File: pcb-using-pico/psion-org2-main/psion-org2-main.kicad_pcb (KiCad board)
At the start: 2 copper layers, 70 x 106 mm, 122 parts, among them J1 Conn_01x24_Female, J2 Conn_01x03_Female, J3 Conn_01x27_Female, J4 Conn_01x02_Female, J5 Conn_01x02_Female, J6 Conn_01x11_Female, M1 P-CH-MOSFET, M2 P-CHANNEL-MOSFET, M3 P-CHANNEL-MOSFET, SW1 AC_ON, SW10 n, SW11 t, SW12 del, SW13 up, SW14 c, SW15 i, SW16 o, SW17 u, SW18 y, SW19 down, SW2 A, SW20 d, SW21 j, SW22 p, SW23 v, SW24 z, SW25 left, SW26 e, SW27 k, SW28 q, SW29 w, SW3 g, SW30 spc, SW31 right, SW32 f, SW33 L, SW34 r, SW35 x, SW36 exe, SW4 m, SW5 s, SW6 shft, SW7 mode, SW8 b, SW9 h, U1 Pico, U10 AMS1117-3.3, U2 74HC595, U3 Regulator_Switching_MT3608, U4 74LS165, U5 74HC595, U7 MCP7940N-xSN, Y1 32k768Hz

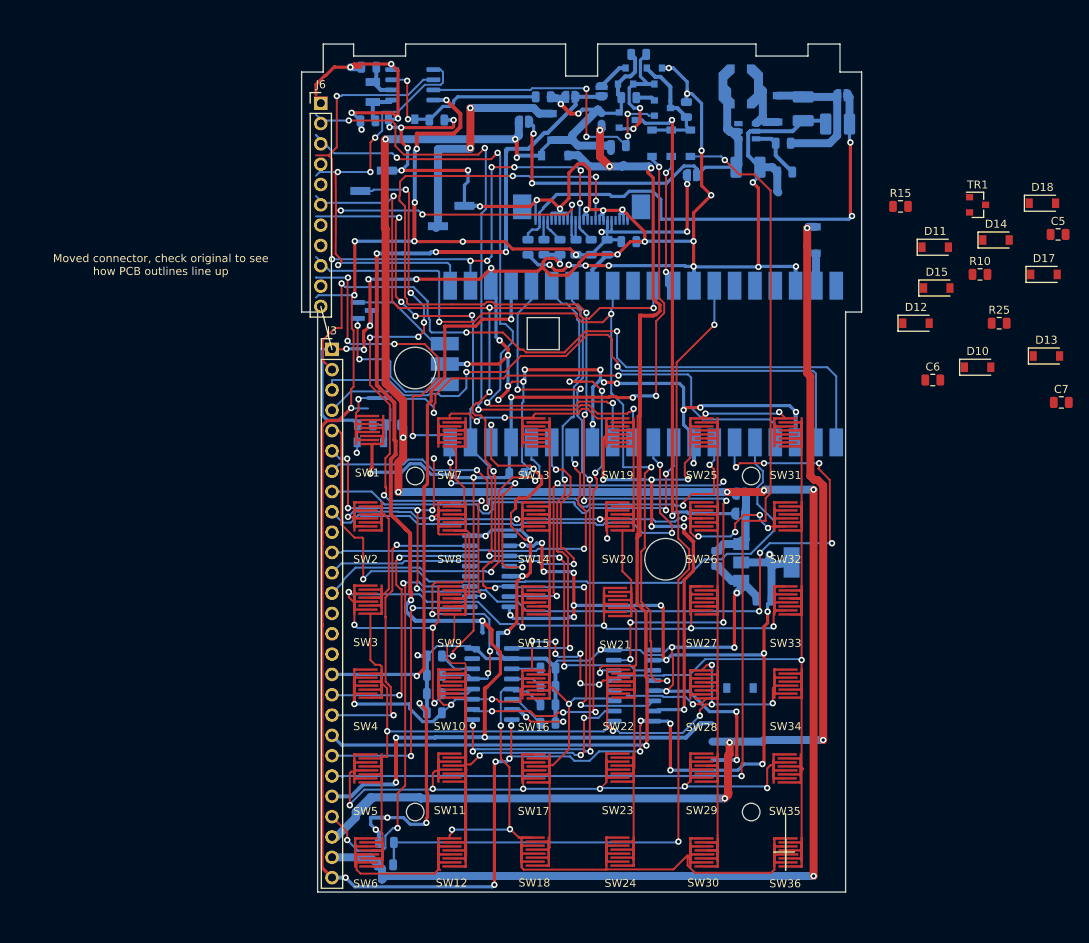
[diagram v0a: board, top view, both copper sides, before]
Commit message: V1.1 PCBs
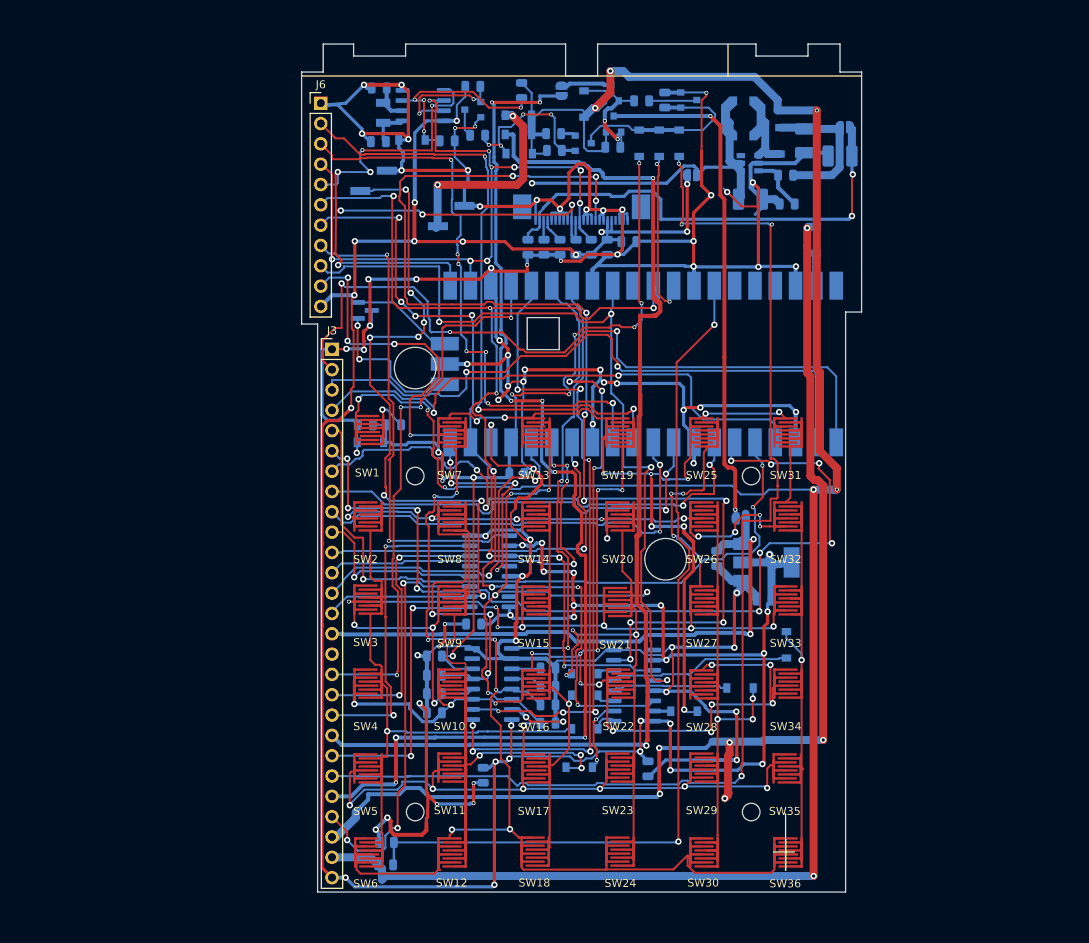
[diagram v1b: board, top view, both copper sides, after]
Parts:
- removed JP3, JP5, JP7: Jumper_NO_Small, Jumper:SolderJumper-2_P1.3mm_Open_RoundedPad1.0x1.5mm
- C5, C6, C7, D10, D11, D12, D13, D14, D15, D17, D18, R10, R15, R25, TR1: moved to B.Cu
- moved C7 86.0 mm to (161.0, 147.1), turned to 270 degrees
- moved C5 84.2 mm to (181.6, 146.3), turned to 270 degrees
- moved D14 84.0 mm to (173.0, 146.1)
- moved D18 82.0 mm to (173.7, 134.4)
- moved D13 74.2 mm to (173.7, 141.3)
- moved R25 72.2 mm to (159.7, 61.0)
- moved D15 67.3 mm to (173.7, 137.1)
- moved R10 65.2 mm to (160.3, 67.1)
- moved C6 65.0 mm to (159.8, 128.2), turned to 180 degrees
- moved TR1 64.2 mm to (159.7, 63.9), turned to 180 degrees
- moved D10 63.2 mm to (165.5, 69.4), turned to 180 degrees
- moved D12 56.5 mm to (186.1, 139.1), turned to 180 degrees
- moved D17 56.4 mm to (198.9, 130.8), turned to 270 degrees
- moved D11 47.4 mm to (173.6, 63.2), turned to 90 degrees
- moved R15 35.0 mm to (180.8, 62.8)
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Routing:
- net P53: track 109.6 -> 192.6 mm, vias 6 -> 12
- net VBAT_SWITCHED1: track 10.4 -> 75.9 mm, vias 0 -> 2
- net QH_O: track 0.00 -> 60.8 mm, vias 0 -> 2
- net P52: track 132.2 -> 186.9 mm, vias 3 -> 7
- net P54: track 121.9 -> 172.5 mm, vias 14 -> 16
- net EXT_PWR_IN: track 207.3 -> 253.9 mm, vias 4 -> 2
- net K6: track 121.3 -> 79.3 mm
- net (no net): track 41.5 -> 0.00 mm, vias 3 -> 0
- net 5V: track 193.7 -> 152.8 mm, vias 4 -> 6
- net VBAT_SWITCHED2: track 174.4 -> 137.5 mm
- net P55: track 146.5 -> 180.0 mm, vias 8 -> 14
- net K4: track 101.3 -> 74.7 mm
- net VBAT: track 285.7 -> 309.4 mm, vias 12 -> 9
- net K3: track 123.8 -> 100.5 mm
- net RTC_MFP: track 38.2 -> 15.3 mm, vias 4 -> 2
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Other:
- outline, holes or cut-outs redrawn
- board text added: "BATCON"
- board text added: "Psion Organiser 2 Re-Creation Main Board menadue@gmail.com Dec 2021 V1.1"
- board text removed: "Moved connector, check original to see how PCB outlines line up"
- board text removed: "Psion Organiser 2 Re Creation Main Board menadue@gmail.com Nov 2021 V1.0"
- board text removed: "VBAT"

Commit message: fab2 V1.1
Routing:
- added copper zone on B.Cu, net GND
- added copper zone on F.Cu, net GND
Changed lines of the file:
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@@
       (drillshape 0)
       (scaleselection 1)
-      (outputdirectory "fab1/"))
+      (outputdirectory "fab2_v1_1/"))
   )
   (net 0 "")
@@
   (segment (start 157.6 110.126998) (end 157.725001 110.251999) (width 0.25) (layer F.Cu) (net 14))
   (segment (start 162.6 136.4) (end 162.6 136.4) (width 0.25) (layer B.Cu) (net 14))
-  (via (at 162.6 136.4) (size 0.5) (drill 0.3) (layers F.Cu B.Cu) (net 14))
+  (via (at 162.6 136.4) (size 0.5) (drill 0.3) (layers F.Cu B.Cu) (net 14) (status 1000000))
   (via (at 162.459662 130.149999) (size 0.5) (drill 0.3) (layers F.Cu B.Cu) (net 14))
   (segment (start 162.6 130.290337) (end 162.459662 130.149999) (width 0.25) (layer F.Cu) (net 14))
@@
   (segment (start 149.7 102.2625) (end 150.7375 103.3) (width 0.25) (layer B.Cu) (net 87))
   (segment (start 149.7 102.134315) (end 149.7 102.2625) (width 0.25) (layer B.Cu) (net 87))
+  (zone (net 1) (net_name GND) (layer F.Cu) (hatch edge 0.508)
+    (connect_pads (clearance 0.508))
+    (min_thickness 0.254)
+    (fill yes (arc_segments 32) (thermal_gap 0.508) (thermal_bridge_width 0.508))
+    (polygon
+      (pts
+        (xy 208.59 54.64) (xy 207.84 163.26) (xy 138.34 163.26) (xy 137.02 54.45)
+      )
+    )
+  )
+  (zone (net 1) (net_name GND) (layer B.Cu) (hatch edge 0.508)
+    (connect_pads (clearance 0.508))
+    (min_thickness 0.254)
+    (fill yes (arc_segments 32) (thermal_gap 0.508) (thermal_bridge_width 0.508))
+    (polygon
+      (pts
+        (xy 209.54 54.3) (xy 208.91 164.79) (xy 136.28 164.79) (xy 136.44 53.73)
+      )
+    )
+  )
 )

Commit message: Updated missing values on schematics, pushed those through to the PCB and created BOM .csv files for those schematics. Created .pdf files for schematics to mitigate the missing library problem of Kicad 5.
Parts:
- C13, C16: value C -> 10pF
- C5, C6, C7: value C_Small -> 100nF
- D2: value D_Schottky -> MBR120VLSFT1G
- D3, D4, D5: value D -> 1N4148
- D8, D9: value D -> AECQ101
- M1: value P-CH-MOSFET -> Si2301
- M2, M3: value P-CHANNEL-MOSFET -> Si2301
- R10, R18, R24: value 110k -> 10k
- R12: value 4k7 -> 5789R
- R13, R14, R15: value 100k -> 10k
- R22: value R_Small -> Not tested or calculated yet
- R23: value R_Small -> Not tested of calculated yet
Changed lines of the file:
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@@
     (add_net "Net-(D7-Pad1)")
     (add_net "Net-(J1-Pad21)")
+    (add_net "Net-(J1-Pad4)")
+    (add_net "Net-(J3-Pad16)")
     (add_net "Net-(JP4-Pad1)")
     (add_net "Net-(JP6-Pad1)")
@@
     (add_net "Net-(R16-Pad1)")
     (add_net "Net-(R22-Pad2)")
+    (add_net "Net-(U1-Pad30)")
+    (add_net "Net-(U1-Pad35)")
+    (add_net "Net-(U1-Pad36)")
+    (add_net "Net-(U1-Pad37)")
+    (add_net "Net-(U1-Pad40)")
+    (add_net "Net-(U2-Pad9)")
+    (add_net "Net-(U3-Pad6)")
+    (add_net "Net-(U4-Pad7)")
+    (add_net "Net-(U5-Pad15)")
+    (add_net "Net-(U5-Pad5)")
     (add_net OLED_RES)
     (add_net OLED_SCL)
@@
       (effects (font (size 1 1) (thickness 0.15)) (justify mirror))
     )
-    (fp_text value 110k (at 0 -1.65) (layer B.Fab)
+    (fp_text value 10k (at 0 -1.65) (layer B.Fab)
       (effects (font (size 1 1) (thickness 0.15)) (justify mirror))
     )
@@
       (effects (font (size 1 1) (thickness 0.15)) (justify mirror))
     )
-    (fp_text value 100k (at 0 -1.65) (layer B.Fab)
+    (fp_text value 10k (at 0 -1.65) (layer B.Fab)
       (effects (font (size 1 1) (thickness 0.15)) (justify mirror))
     )
@@
       (effects (font (size 1 1) (thickness 0.15)) (justify mirror))
     )
-    (fp_text value 110k (at 0 -1.65) (layer B.Fab)
+    (fp_text value 10k (at 0 -1.65) (layer B.Fab)
       (effects (font (size 1 1) (thickness 0.15)) (justify mirror))
     )
@@
       (effects (font (size 1 1) (thickness 0.15)) (justify mirror))
     )
-    (fp_text value C_Small (at 0 -1.65 90) (layer B.Fab)
+    (fp_text value 100nF (at 0 -1.65 90) (layer B.Fab)
       (effects (font (size 1 1) (thickness 0.15)) (justify mirror))
     )
@@
       (effects (font (size 1 1) (thickness 0.15)) (justify mirror))
     )
-    (fp_text value C_Small (at 0 -1.65) (layer B.Fab)
+    (fp_text value 100nF (at 0 -1.65) (layer B.Fab)
       (effects (font (size 1 1) (thickness 0.15)) (justify mirror))
     )
@@
       (effects (font (size 1 1) (thickness 0.15)) (justify mirror))
     )
-    (fp_text value C_Small (at 0 -1.65 90) (layer B.Fab)
+    (fp_text value 100nF (at 0 -1.65 90) (layer B.Fab)
       (effects (font (size 1 1) (thickness 0.15)) (justify mirror))
     )
@@
       (effects (font (size 1 1) (thickness 0.15)) (justify mirror))
     )
-    (fp_text value D (at 0 -2.1) (layer B.Fab)
+    (fp_text value AECQ101 (at 0 -2.1) (layer B.Fab)
       (effects (font (size 1 1) (thickness 0.15)) (justify mirror))
     )
@@
       (effects (font (size 1 1) (thickness 0.15)) (justify mirror))
     )
-    (fp_text value D (at 0 -2.1) (layer B.Fab)
+    (fp_text value AECQ101 (at 0 -2.1) (layer B.Fab)
       (effects (font (size 1 1) (thickness 0.15)) (justify mirror))
     )
@@
       (effects (font (size 1 1) (thickness 0.15)) (justify mirror))
     )
-    (fp_text value 110k (at 0 -1.65) (layer B.Fab)
+    (fp_text value 10k (at 0 -1.65) (layer B.Fab)
       (effects (font (size 1 1) (thickness 0.15)) (justify mirror))
     )
@@
       (effects (font (size 1 1) (thickness 0.15)) (justify mirror))
     )
-    (fp_text value P-CHANNEL-MOSFET (at 0 -2.5 90) (layer B.Fab)
+    (fp_text value Si2301 (at 0 -2.5 90) (layer B.Fab)
       (effects (font (size 1 1) (thickness 0.15)) (justify mirror))
     )
@@
       (effects (font (size 1 1) (thickness 0.15)) (justify mirror))
     )
-    (fp_text value C (at 0 -1.65) (layer B.Fab)
+    (fp_text value 10pF (at 0 -1.65) (layer B.Fab)
       (effects (font (size 1 1) (thickness 0.15)) (justify mirror))
     )
@@
       (effects (font (size 1 1) (thickness 0.15)) (justify mirror))
     )
-    (fp_text value C (at 0 -1.65) (layer B.Fab)
+    (fp_text value 10pF (at 0 -1.65) (layer B.Fab)
       (effects (font (size 1 1) (thickness 0.15)) (justify mirror))
     )
@@
       (effects (font (size 1 1) (thickness 0.15)) (justify mirror))
     )
-    (fp_text value P-CHANNEL-MOSFET (at 0 -2.5 90) (layer B.Fab)
+    (fp_text value Si2301 (at 0 -2.5 90) (layer B.Fab)
       (effects (font (size 1 1) (thickness 0.15)) (justify mirror))
     )
@@
       (effects (font (size 1 1) (thickness 0.15)) (justify mirror))
     )
-    (fp_text value P-CH-MOSFET (at 0 -2.5) (layer B.Fab)
+    (fp_text value Si2301 (at 0 -2.5) (layer B.Fab)
       (effects (font (size 1 1) (thickness 0.15)) (justify mirror))
     )
@@
       (effects (font (size 1 1) (thickness 0.15)) (justify mirror))
     )
-    (fp_text value 100k (at 0 -1.65) (layer B.Fab)
+    (fp_text value 10k (at 0 -1.65) (layer B.Fab)
       (effects (font (size 1 1) (thickness 0.15)) (justify mirror))
     )
@@
       (effects (font (size 1 1) (thickness 0.15)) (justify mirror))
     )
-    (fp_text value 100k (at 0 -1.65 90) (layer B.Fab)
+    (fp_text value 10k (at 0 -1.65 90) (layer B.Fab)
       (effects (font (size 1 1) (thickness 0.15)) (justify mirror))
     )
@@
       (effects (font (size 1 1) (thickness 0.15)) (justify mirror))
     )
-    (fp_text value D (at 0 -2.1 90) (layer B.Fab)
+    (fp_text value 1N4148 (at 0 -2.1 90) (layer B.Fab)
       (effects (font (size 1 1) (thickness 0.15)) (justify mirror))
     )
@@
       (effects (font (size 1 1) (thickness 0.15)) (justify mirror))
     )
-    (fp_text value D (at 0 -2.1 90) (layer B.Fab)
+    (fp_text value 1N4148 (at 0 -2.1 90) (layer B.Fab)
       (effects (font (size 1 1) (thickness 0.15)) (justify mirror))
     )
@@
       (effects (font (size 1 1) (thickness 0.15)) (justify mirror))
     )
-    (fp_text value D (at 0 -2.1 90) (layer B.Fab)
+    (fp_text value 1N4148 (at 0 -2.1 90) (layer B.Fab)
       (effects (font (size 1 1) (thickness 0.15)) (justify mirror))
     )
@@
       (effects (font (size 1 1) (thickness 0.15)) (justify mirror))
     )
-    (fp_text value D_Schottky (at 0 -2.1 90) (layer B.Fab)
+    (fp_text value MBR120VLSFT1G (at 0 -2.1 90) (layer B.Fab)
       (effects (font (size 1 1) (thickness 0.15)) (justify mirror))
     )
@@
       (effects (font (size 1 1) (thickness 0.15)) (justify mirror))
     )
-    (fp_text value R_Small (at 0 -1.65) (layer B.Fab)
+    (fp_text value "Not tested of calculated yet" (at 0 -1.65) (layer B.Fab)
       (effects (font (size 1 1) (thickness 0.15)) (justify mirror))
     )
@@
       (effects (font (size 1 1) (thickness 0.15)) (justify mirror))
     )
-    (fp_text value R_Small (at 0 -1.65) (layer B.Fab)
+    (fp_text value "Not tested or calculated yet" (at 0 -1.65) (layer B.Fab)
       (effects (font (size 1 1) (thickness 0.15)) (justify mirror))
     )
@@
       (effects (font (size 1 1) (thickness 0.15)) (justify mirror))
     )
-    (fp_text value 4k7 (at 0 -1.65) (layer B.Fab)
+    (fp_text value 5789R (at 0 -1.65) (layer B.Fab)
       (effects (font (size 1 1) (thickness 0.15)) (justify mirror))
     )

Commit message: Updates
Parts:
- added C11: 100nF, Capacitor_SMD:C_0805_2012Metric, B.Cu at (177.5, 70.6)
- added C8: 100nF, Capacitor_SMD:C_0805_2012Metric, B.Cu at (180.8, 60.7)
- added C9: 100nF, Capacitor_SMD:C_0805_2012Metric, B.Cu at (169.9, 70.6)
- added D19: nopop, Diode_SMD:D_SOD-123, B.Cu at (163.3, 60.2)
- added R26: 10k, Resistor_SMD:R_0805_2012Metric, B.Cu at (156.0, 59.6)
- moved R24 0.86 mm to (169.8, 66.0)
- moved R18 0.67 mm to (169.9, 68.3)
- moved R25 0.18 mm to (159.6, 60.8)
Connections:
- R25 pad 1: +3V3 -> VBAT
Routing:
- net VBAT: track 309.4 -> 332.3 mm
- net GND: track 623.1 -> 636.1 mm
- net RTC_MFP: track 15.3 -> 23.6 mm
- net Net-(C8-Pad1): track 24.9 -> 31.4 mm
- net +3V3: track 356.5 -> 350.2 mm, vias 33 -> 32
- net OLED_RES: track 144.5 -> 147.1 mm
- net Net-(C9-Pad2): track 20.6 -> 22.9 mm
- net Net-(C11-Pad2): track 16.3 -> 18.5 mm
- net EXT_PWR_IN: track 253.9 -> 255.3 mm
- net OLED_SCL: track 86.3 -> 87.2 mm
- net Net-(M1-Pad2): track 1.87 -> 2.73 mm
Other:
- board text added: "Psion Organiser 2 Re-Creation Main Board menadue@gmail.com Sep 2022 V1.2"
- board text removed: "Psion Organiser 2 Re-Creation Main Board menadue@gmail.com Dec 2021 V1.1"
